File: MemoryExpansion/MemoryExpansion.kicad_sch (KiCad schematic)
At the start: 9 parts, among them J1 1.5MB RAM Expansion, U1 74LS139, U2 AS6C4008-55PCN, U3 AS6C4008-55PCN, U4 AS6C4008-55PCN

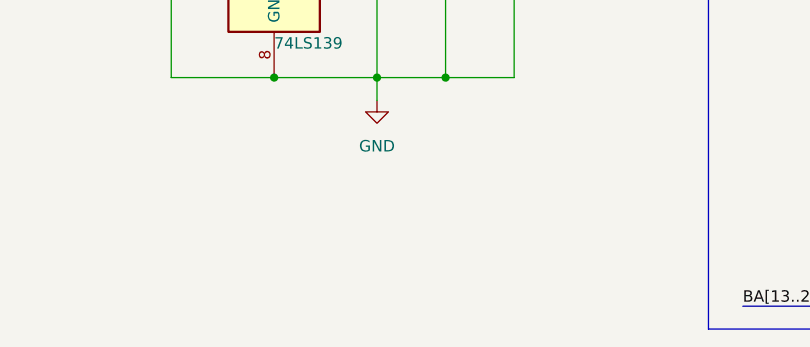
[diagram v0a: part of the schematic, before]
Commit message: Change 2.2u cap footprint; update MemoryExpansion
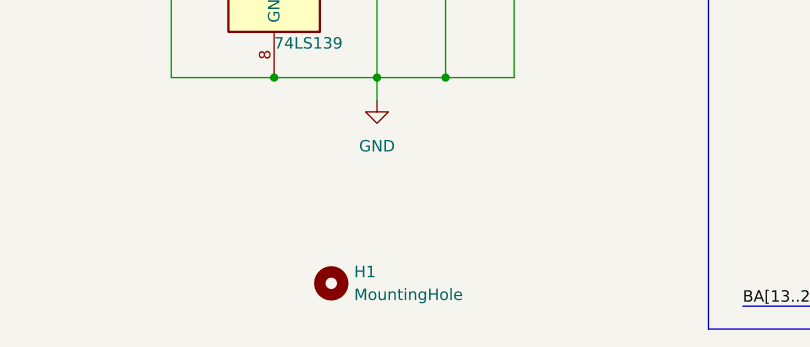
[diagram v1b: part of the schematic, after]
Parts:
- added H1: MountingHole, MountingHole:MountingHole_2.2mm_M2, symbol Mechanical:MountingHole
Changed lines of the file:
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@@
+	)
+	(symbol
+		(lib_id "Mechanical:MountingHole")
+		(at 82.55 156.21 0)
+		(unit 1)
+		(exclude_from_sim yes)
+		(in_bom no)
+		(on_board yes)
+		(dnp no)
+		(fields_autoplaced yes)
+		(property "Reference" "H1"
+			(at 85.09 154.9399 0)
+			(effects
+				(font
+					(size 1.27 1.27)
+				)
+				(justify left)
+			)
+		)
+		(property "Value" "MountingHole"
+			(at 85.09 157.4799 0)
+			(effects
+				(font
+					(size 1.27 1.27)
+				)
+				(justify left)
+			)
+		)
+		(property "Footprint" "MountingHole:MountingHole_2.2mm_M2"
+			(at 82.55 156.21 0)
+			(effects
+				(font
+					(size 1.27 1.27)
+				)
+				(hide yes)
+			)
+		)
+		(property "Datasheet" "~"
+			(at 82.55 156.21 0)
+			(effects
+				(font
+					(size 1.27 1.27)
+				)
+				(hide yes)
+			)
+		)
+		(property "Description" "Mounting Hole without connection"
+			(at 82.55 156.21 0)
+			(effects
+				(font
+					(size 1.27 1.27)
+				)
+				(hide yes)
+			)
+		)
+		(instances
+			(project ""
+				(path "/05473346-b5e4-4a9d-a4b0-c699590ad832"
+					(reference "H1")
+					(unit 1)
+				)
+			)
+		)
 	)
 	(symbol
